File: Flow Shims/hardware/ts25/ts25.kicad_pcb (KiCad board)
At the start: 4 copper layers, 76.8 x 114 mm, 150 parts, among them J2 Nano-Fit, Q10 NVTFS5116PL, Q11 NVTFS5116PL, Q12 NVTFS5116PL, Q13 NVTFS5116PL, Q14 NVTFS5116PL, Q15 NVTFS5116PL, Q16 NVTFS5116PL, Q17 NVTFS5116PL, Q18 NVTFS5116PL, Q19 NVTFS5116PL, Q20 NVTFS5116PL, Q21 NVTFS5116PL, Q22 NVTFS5116PL, Q23 NVTFS5116PL, Q24 NVTFS5116PL, Q25 NVTFS5116PL, Q26 NVTFS5116PL, Q27 NVTFS5116PL, Q28 NVTFS5116PL, Q29 NVTFS5116PL, Q30 NVTFS5116PL, Q31 NVTFS5116PL, Q32 NVTFS5116PL, Q33 NVTFS5116PL, Q9 NVTFS5116PL, U1 ADG5206, U10 TMP1826NG, U11 TMP1826NG, U12 TMP1826NG, U13 TMP1826NG, U14 TMP1826NG, U15 TMP1826NG, U16 TMP1826NG, U17 TMP1826NG, U18 TMP1826NG, U19 TMP1826NG, U2 TMP1826NG, U20 TMP1826NG, U21 TMP1826NG, U22 TMP1826NG, U23 TMP1826NG, U24 TMP1826NG, U25 TMP1826NG, U26 TMP1826NG, U27 ADG5206, U3 TMP1826NG, U4 TMP1826NG, U5 TMP1826NG, U53 OPA196xDBV, U54 OPA196xDBV, U55 OPA196xDBV, U56 OPA196xDBV, U57 OPA196xDBV, U58 OPA196xDBV, U59 OPA196xDBV, U6 TMP1826NG, U60 OPA196xDBV, U61 OPA196xDBV, U62 OPA196xDBV, U63 OPA196xDBV, U64 OPA196xDBV, U65 OPA196xDBV, U66 OPA196xDBV, U67 OPA196xDBV, U68 OPA196xDBV, U69 OPA196xDBV, U7 TMP1826NG, U70 OPA196xDBV, U71 OPA196xDBV, U72 OPA196xDBV, U73 OPA196xDBV, U74 OPA196xDBV, U75 OPA196xDBV, U76 OPA196xDBV, U77 OPA196xDBV, U78 OPA196xDBV, U79 OPA196xDBV, U8 TMP1826NG, U9 TMP1826NG

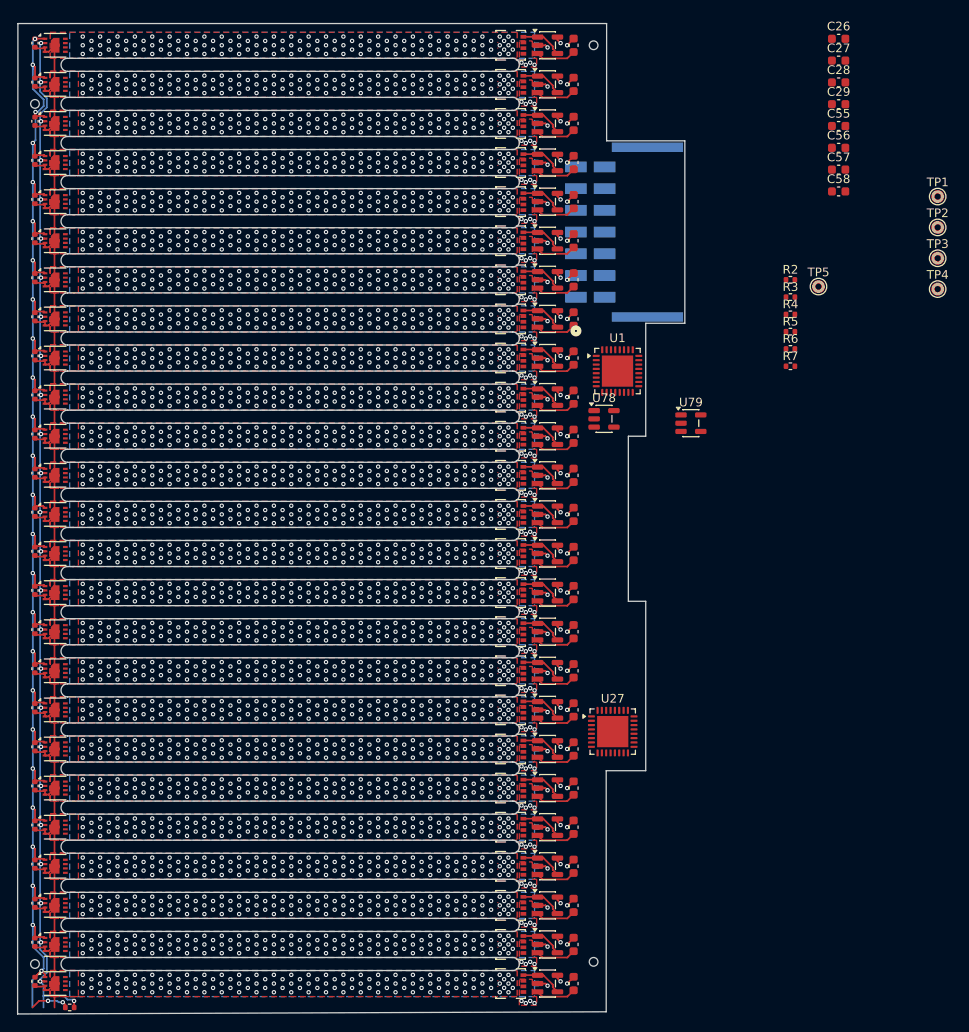
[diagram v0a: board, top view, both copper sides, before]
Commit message: DRC clean, single heater
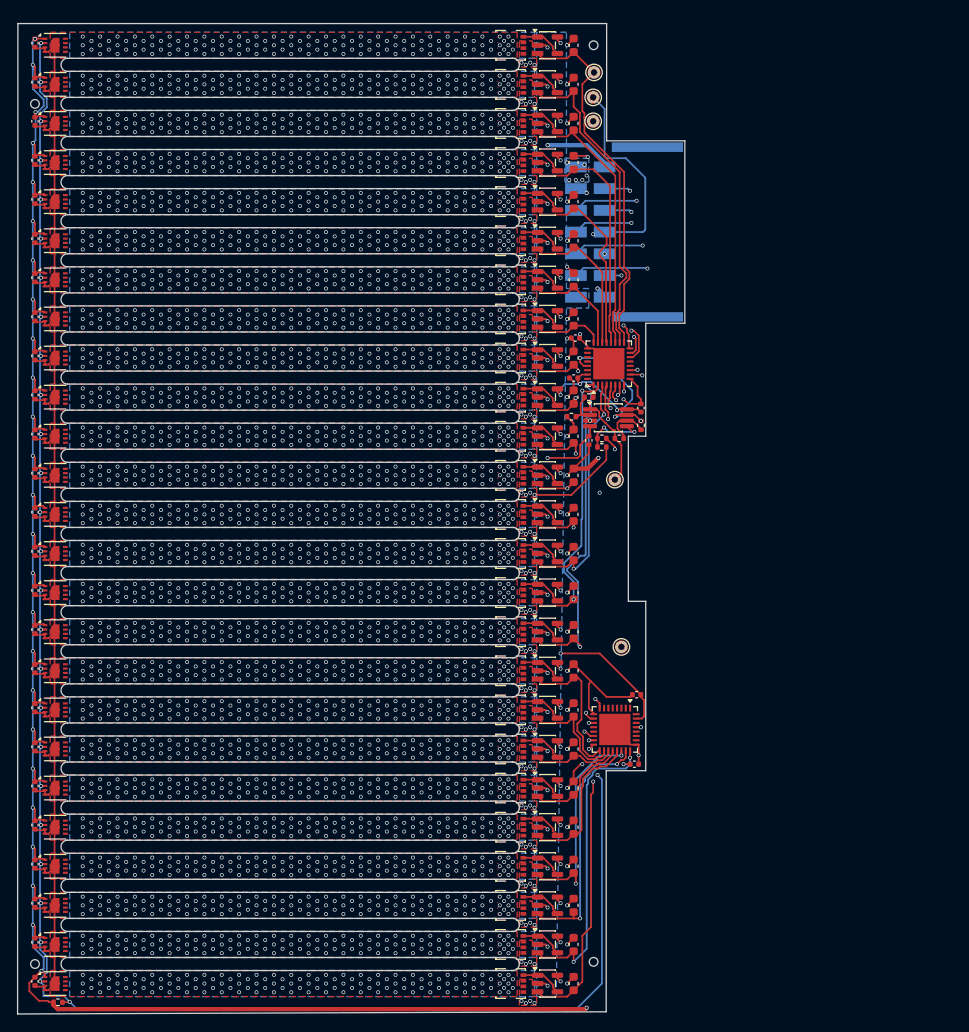
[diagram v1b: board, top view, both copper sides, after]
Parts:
- removed C55, C58: 100n, Capacitor_SMD:C_0603_1608Metric
- removed U78, U79: OPA196xDBV, Package_TO_SOT_SMD:SOT-23-5
- added U28: OPA2196xDGK, Package_SO:VSSOP-8_3x3mm_P0.65mm, F.Cu at (173.0, 86.4)
- C26, C27, C28, C29, C56, C57: footprint Capacitor_SMD:C_0603_1608Metric -> Capacitor_SMD:C_0402_1005Metric
- moved C26 86.7 mm to (176.0, 126.2)
- moved C28 74.2 mm to (176.2, 118.2)
- moved TP4 55.0 mm to (174.5, 112.8)
- moved TP3 45.1 mm to (173.8, 93.5)
- moved C27 44.0 mm to (169.2, 77.2)
- moved C29 43.9 mm to (169.0, 81.8)
- moved C57 42.4 mm to (170.8, 89.0), turned to -90 degrees
- moved TP2 42.4 mm to (171.2, 49.5)
- moved TP1 40.6 mm to (171.2, 52.2)
- moved C56 37.6 mm to (176.8, 85.2), turned to 90 degrees
- moved TP5 35.7 mm to (171.3, 46.6)
- moved R3 28.7 mm to (168.8, 86.2)
- moved R2 26.8 mm to (170.8, 84.0)
- moved R4 26.0 mm to (172.2, 88.8), turned to 180 degrees
- moved R5 25.4 mm to (172.2, 89.8)
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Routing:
- net GND: track 217.1 -> 375.3 mm, vias 3275 -> 3281
- net +3.3V: track 187.4 -> 342.4 mm
- net -15V: track 31.0 -> 182.9 mm, vias 25 -> 29
- net /VTEMP: track 131.7 -> 278.2 mm, vias 26 -> 29
- net +15V: track 21.3 -> 164.7 mm, vias 25 -> 29
- net /A0: track 0.00 -> 76.0 mm, vias 0 -> 3
- net /A1: track 0.00 -> 74.3 mm, vias 0 -> 3
- net /EN1: track 0.00 -> 73.8 mm, vias 0 -> 2
- net /A2: track 0.00 -> 67.8 mm, vias 0 -> 3
- net /A3: track 0.00 -> 65.4 mm, vias 0 -> 3
- net /VG: track 0.00 -> 54.3 mm, vias 0 -> 4
- net /VGIN: track 0.00 -> 47.2 mm, vias 0 -> 2
- net /VG1: track 4.67 -> 42.6 mm
- net /VG25: track 4.67 -> 40.6 mm, vias 0 -> 2
- net /VG16: track 4.67 -> 39.2 mm, vias 0 -> 2
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- added copper zone on B.Cu, net VD
- added copper zone on In1.Cu, net VD

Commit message: Building code for heater control PID loops
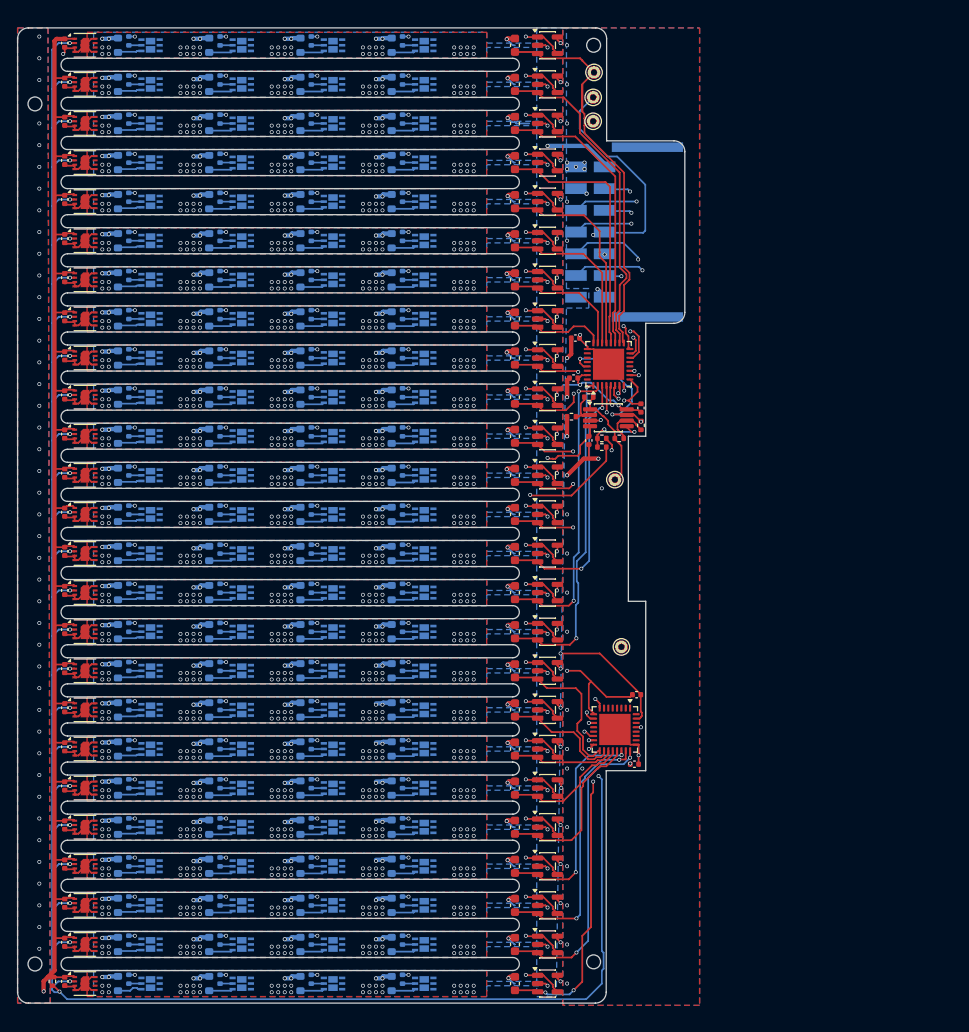
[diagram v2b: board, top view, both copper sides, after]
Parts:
- removed Q10, Q11, Q12, Q13, Q14, Q15, Q16, Q17, Q18, Q19, Q20, Q21, Q22, Q23, Q24, Q25, Q26, Q27, Q28, Q29, Q30, Q31, Q32, Q33, Q9: NVTFS5116PL, thermalshims:WDFN8_511AB_ONS_OSI
- added R10: 5, Resistor_SMD:R_0603_1608Metric, B.Cu at (116.6, 52.5)
- added R100: 10, Resistor_SMD:R_0402_1005Metric, B.Cu at (128.3, 137.5)
- added R101: 5, Resistor_SMD:R_0603_1608Metric, B.Cu at (127.1, 138.0)
- added R102: 10, Resistor_SMD:R_0402_1005Metric, B.Cu at (128.3, 142.0)
- added R103: 5, Resistor_SMD:R_0603_1608Metric, B.Cu at (127.1, 142.5)
- added R104: 10, Resistor_SMD:R_0402_1005Metric, B.Cu at (128.3, 146.5)
- added R105: 5, Resistor_SMD:R_0603_1608Metric, B.Cu at (127.1, 147.0)
- added R106: 10, Resistor_SMD:R_0402_1005Metric, B.Cu at (128.3, 151.0)
- added R107: 5, Resistor_SMD:R_0603_1608Metric, B.Cu at (127.1, 151.5)
- added R108: 10, Resistor_SMD:R_0402_1005Metric, B.Cu at (138.8, 43.0)
- added R109: 5, Resistor_SMD:R_0603_1608Metric, B.Cu at (137.6, 43.5)
- added R11: 5, Resistor_SMD:R_0603_1608Metric, B.Cu at (116.6, 57.0)
- added R110: 10, Resistor_SMD:R_0402_1005Metric, B.Cu at (138.8, 47.5)
- added R111: 5, Resistor_SMD:R_0603_1608Metric, B.Cu at (137.6, 48.0)
- added R112: 10, Resistor_SMD:R_0402_1005Metric, B.Cu at (138.8, 52.0)
- added R113: 5, Resistor_SMD:R_0603_1608Metric, B.Cu at (137.6, 52.5)
- added R114: 10, Resistor_SMD:R_0402_1005Metric, B.Cu at (138.8, 56.5)
- added R115: 5, Resistor_SMD:R_0603_1608Metric, B.Cu at (137.6, 57.0)
- added R116: 10, Resistor_SMD:R_0402_1005Metric, B.Cu at (138.8, 61.0)
- added R117: 5, Resistor_SMD:R_0603_1608Metric, B.Cu at (137.6, 61.5)
- added R118: 10, Resistor_SMD:R_0402_1005Metric, B.Cu at (138.8, 65.5)
- added R119: 5, Resistor_SMD:R_0603_1608Metric, B.Cu at (137.6, 66.0)
- added R12: 5, Resistor_SMD:R_0603_1608Metric, B.Cu at (116.6, 61.5)
- added R120: 10, Resistor_SMD:R_0402_1005Metric, B.Cu at (138.8, 70.0)
- added R121: 5, Resistor_SMD:R_0603_1608Metric, B.Cu at (137.6, 70.5)
- added R122: 10, Resistor_SMD:R_0402_1005Metric, B.Cu at (138.8, 74.5)
- added R123: 5, Resistor_SMD:R_0603_1608Metric, B.Cu at (137.6, 75.0)
- added R124: 10, Resistor_SMD:R_0402_1005Metric, B.Cu at (138.8, 79.0)
- added R125: 5, Resistor_SMD:R_0603_1608Metric, B.Cu at (137.6, 79.5)
- added R126: 10, Resistor_SMD:R_0402_1005Metric, B.Cu at (138.8, 83.5)
- added R127: 5, Resistor_SMD:R_0603_1608Metric, B.Cu at (137.6, 84.0)
- added R128: 10, Resistor_SMD:R_0402_1005Metric, B.Cu at (138.8, 88.0)
- added R129: 5, Resistor_SMD:R_0603_1608Metric, B.Cu at (137.6, 88.5)
- added R13: 5, Resistor_SMD:R_0603_1608Metric, B.Cu at (116.6, 66.0)
- added R130: 10, Resistor_SMD:R_0402_1005Metric, B.Cu at (138.8, 92.5)
- added R131: 5, Resistor_SMD:R_0603_1608Metric, B.Cu at (137.6, 93.0)
- added R132: 10, Resistor_SMD:R_0402_1005Metric, B.Cu at (138.8, 97.0)
- added R133: 5, Resistor_SMD:R_0603_1608Metric, B.Cu at (137.6, 97.5)
- added R134: 10, Resistor_SMD:R_0402_1005Metric, B.Cu at (138.8, 101.5)
- added R135: 5, Resistor_SMD:R_0603_1608Metric, B.Cu at (137.6, 102.0)
- added R136: 10, Resistor_SMD:R_0402_1005Metric, B.Cu at (138.8, 106.0)
- added R137: 5, Resistor_SMD:R_0603_1608Metric, B.Cu at (137.6, 106.5)
- added R138: 10, Resistor_SMD:R_0402_1005Metric, B.Cu at (138.8, 110.5)
- added R139: 5, Resistor_SMD:R_0603_1608Metric, B.Cu at (137.6, 111.0)
- added R14: 5, Resistor_SMD:R_0603_1608Metric, B.Cu at (116.6, 70.5)
- added R140: 10, Resistor_SMD:R_0402_1005Metric, B.Cu at (138.8, 115.0)
- added R141: 5, Resistor_SMD:R_0603_1608Metric, B.Cu at (137.6, 115.5)
- added R142: 10, Resistor_SMD:R_0402_1005Metric, B.Cu at (138.8, 119.5)
- added R143: 5, Resistor_SMD:R_0603_1608Metric, B.Cu at (137.6, 120.0)
- added R144: 10, Resistor_SMD:R_0402_1005Metric, B.Cu at (138.8, 124.0)
- added R145: 5, Resistor_SMD:R_0603_1608Metric, B.Cu at (137.6, 124.5)
- added R146: 10, Resistor_SMD:R_0402_1005Metric, B.Cu at (138.8, 128.5)
- added R147: 5, Resistor_SMD:R_0603_1608Metric, B.Cu at (137.6, 129.0)
- added R148: 10, Resistor_SMD:R_0402_1005Metric, B.Cu at (138.8, 133.0)
- added R149: 5, Resistor_SMD:R_0603_1608Metric, B.Cu at (137.6, 133.5)
- added R15: 5, Resistor_SMD:R_0603_1608Metric, B.Cu at (116.6, 75.0)
- added R150: 10, Resistor_SMD:R_0402_1005Metric, B.Cu at (138.8, 137.5)
- added R151: 5, Resistor_SMD:R_0603_1608Metric, B.Cu at (137.6, 138.0)
- added R152: 10, Resistor_SMD:R_0402_1005Metric, B.Cu at (138.8, 142.0)
- added R153: 5, Resistor_SMD:R_0603_1608Metric, B.Cu at (137.6, 142.5)
- added R154: 10, Resistor_SMD:R_0402_1005Metric, B.Cu at (138.8, 146.5)
- added R155: 5, Resistor_SMD:R_0603_1608Metric, B.Cu at (137.6, 147.0)
- added R156: 10, Resistor_SMD:R_0402_1005Metric, B.Cu at (138.8, 151.0)
- added R157: 5, Resistor_SMD:R_0603_1608Metric, B.Cu at (137.6, 151.5)
- added R158: 10, Resistor_SMD:R_0402_1005Metric, B.Cu at (149.3, 43.0)
- added R159: 5, Resistor_SMD:R_0603_1608Metric, B.Cu at (148.1, 43.5)
- added R16: 5, Resistor_SMD:R_0603_1608Metric, B.Cu at (116.6, 79.5)
- added R160: 10, Resistor_SMD:R_0402_1005Metric, B.Cu at (149.3, 47.5)
- added R161: 5, Resistor_SMD:R_0603_1608Metric, B.Cu at (148.1, 48.0)
- added R162: 10, Resistor_SMD:R_0402_1005Metric, B.Cu at (149.3, 52.0)
- added R163: 5, Resistor_SMD:R_0603_1608Metric, B.Cu at (148.1, 52.5)
- added R164: 10, Resistor_SMD:R_0402_1005Metric, B.Cu at (149.3, 56.5)
- added R165: 5, Resistor_SMD:R_0603_1608Metric, B.Cu at (148.1, 57.0)
- added R166: 10, Resistor_SMD:R_0402_1005Metric, B.Cu at (149.3, 61.0)
- added R167: 5, Resistor_SMD:R_0603_1608Metric, B.Cu at (148.1, 61.5)
- added R168: 10, Resistor_SMD:R_0402_1005Metric, B.Cu at (149.3, 65.5)
- added R169: 5, Resistor_SMD:R_0603_1608Metric, B.Cu at (148.1, 66.0)
- added R17: 5, Resistor_SMD:R_0603_1608Metric, B.Cu at (116.6, 84.0)
- added R170: 10, Resistor_SMD:R_0402_1005Metric, B.Cu at (149.3, 70.0)
- added R171: 5, Resistor_SMD:R_0603_1608Metric, B.Cu at (148.1, 70.5)
- added R172: 10, Resistor_SMD:R_0402_1005Metric, B.Cu at (149.3, 74.5)
- added R173: 5, Resistor_SMD:R_0603_1608Metric, B.Cu at (148.1, 75.0)
- added R174: 10, Resistor_SMD:R_0402_1005Metric, B.Cu at (149.3, 79.0)
- added R175: 5, Resistor_SMD:R_0603_1608Metric, B.Cu at (148.1, 79.5)
- added R176: 10, Resistor_SMD:R_0402_1005Metric, B.Cu at (149.3, 83.5)
- added R177: 5, Resistor_SMD:R_0603_1608Metric, B.Cu at (148.1, 84.0)
- added R178: 10, Resistor_SMD:R_0402_1005Metric, B.Cu at (149.3, 88.0)
- added R179: 5, Resistor_SMD:R_0603_1608Metric, B.Cu at (148.1, 88.5)
- added R18: 5, Resistor_SMD:R_0603_1608Metric, B.Cu at (116.6, 88.5)
- added R180: 10, Resistor_SMD:R_0402_1005Metric, B.Cu at (149.3, 92.5)
- added R181: 5, Resistor_SMD:R_0603_1608Metric, B.Cu at (148.1, 93.0)
- added R182: 10, Resistor_SMD:R_0402_1005Metric, B.Cu at (149.3, 97.0)
- added R183: 5, Resistor_SMD:R_0603_1608Metric, B.Cu at (148.1, 97.5)
- added R184: 10, Resistor_SMD:R_0402_1005Metric, B.Cu at (149.3, 101.5)
- added R185: 5, Resistor_SMD:R_0603_1608Metric, B.Cu at (148.1, 102.0)
- added R186: 10, Resistor_SMD:R_0402_1005Metric, B.Cu at (149.3, 106.0)
- added R187: 5, Resistor_SMD:R_0603_1608Metric, B.Cu at (148.1, 106.5)
- added R188: 10, Resistor_SMD:R_0402_1005Metric, B.Cu at (149.3, 110.5)
- added R189: 5, Resistor_SMD:R_0603_1608Metric, B.Cu at (148.1, 111.0)
- added R19: 5, Resistor_SMD:R_0603_1608Metric, B.Cu at (116.6, 93.0)
- added R190: 10, Resistor_SMD:R_0402_1005Metric, B.Cu at (149.3, 115.0)
- added R191: 5, Resistor_SMD:R_0603_1608Metric, B.Cu at (148.1, 115.5)
- added R192: 10, Resistor_SMD:R_0402_1005Metric, B.Cu at (149.3, 119.5)
- added R193: 5, Resistor_SMD:R_0603_1608Metric, B.Cu at (148.1, 120.0)
- added R194: 10, Resistor_SMD:R_0402_1005Metric, B.Cu at (149.3, 124.0)
- added R195: 5, Resistor_SMD:R_0603_1608Metric, B.Cu at (148.1, 124.5)
- added R196: 10, Resistor_SMD:R_0402_1005Metric, B.Cu at (149.3, 128.5)
- added R197: 5, Resistor_SMD:R_0603_1608Metric, B.Cu at (148.1, 129.0)
- added R198: 10, Resistor_SMD:R_0402_1005Metric, B.Cu at (149.3, 133.0)
- added R199: 5, Resistor_SMD:R_0603_1608Metric, B.Cu at (148.1, 133.5)
- added R20: 5, Resistor_SMD:R_0603_1608Metric, B.Cu at (116.6, 97.5)
- added R200: 10, Resistor_SMD:R_0402_1005Metric, B.Cu at (149.3, 137.5)
- added R201: 5, Resistor_SMD:R_0603_1608Metric, B.Cu at (148.1, 138.0)
- added R202: 10, Resistor_SMD:R_0402_1005Metric, B.Cu at (149.3, 142.0)
- added R203: 5, Resistor_SMD:R_0603_1608Metric, B.Cu at (148.1, 142.5)
- added R204: 10, Resistor_SMD:R_0402_1005Metric, B.Cu at (149.3, 146.5)
- added R205: 5, Resistor_SMD:R_0603_1608Metric, B.Cu at (148.1, 147.0)
- added R206: 10, Resistor_SMD:R_0402_1005Metric, B.Cu at (149.3, 151.0)
- added R207: 5, Resistor_SMD:R_0603_1608Metric, B.Cu at (148.1, 151.5)
- added R21: 5, Resistor_SMD:R_0603_1608Metric, B.Cu at (116.6, 102.0)
- added R22: 5, Resistor_SMD:R_0603_1608Metric, B.Cu at (116.6, 106.5)
- added R23: 5, Resistor_SMD:R_0603_1608Metric, B.Cu at (116.6, 111.0)
- added R24: 5, Resistor_SMD:R_0603_1608Metric, B.Cu at (116.6, 115.5)
- added R25: 5, Resistor_SMD:R_0603_1608Metric, B.Cu at (116.6, 120.0)
- added R26: 5, Resistor_SMD:R_0603_1608Metric, B.Cu at (116.6, 124.5)
- added R27: 5, Resistor_SMD:R_0603_1608Metric, B.Cu at (116.6, 129.0)
- added R28: 5, Resistor_SMD:R_0603_1608Metric, B.Cu at (116.6, 133.5)
- added R29: 5, Resistor_SMD:R_0603_1608Metric, B.Cu at (116.6, 138.0)
- added R30: 5, Resistor_SMD:R_0603_1608Metric, B.Cu at (116.6, 142.5)
- added R31: 5, Resistor_SMD:R_0603_1608Metric, B.Cu at (116.6, 147.0)
- added R32: 5, Resistor_SMD:R_0603_1608Metric, B.Cu at (116.6, 151.5)
- added R33: 10, Resistor_SMD:R_0402_1005Metric, B.Cu at (117.8, 43.0)
- added R34: 10, Resistor_SMD:R_0402_1005Metric, B.Cu at (117.8, 47.5)
- added R35: 10, Resistor_SMD:R_0402_1005Metric, B.Cu at (117.8, 52.0)
- added R36: 10, Resistor_SMD:R_0402_1005Metric, B.Cu at (117.8, 56.5)
- added R37: 10, Resistor_SMD:R_0402_1005Metric, B.Cu at (117.8, 61.0)
- added R38: 10, Resistor_SMD:R_0402_1005Metric, B.Cu at (117.8, 65.5)
- added R39: 10, Resistor_SMD:R_0402_1005Metric, B.Cu at (117.8, 70.0)
- added R40: 10, Resistor_SMD:R_0402_1005Metric, B.Cu at (117.8, 74.5)
- added R41: 10, Resistor_SMD:R_0402_1005Metric, B.Cu at (117.8, 79.0)
- added R42: 10, Resistor_SMD:R_0402_1005Metric, B.Cu at (117.8, 83.5)
- added R43: 10, Resistor_SMD:R_0402_1005Metric, B.Cu at (117.8, 88.0)
- added R44: 10, Resistor_SMD:R_0402_1005Metric, B.Cu at (117.8, 92.5)
- added R45: 10, Resistor_SMD:R_0402_1005Metric, B.Cu at (117.8, 97.0)
- added R46: 10, Resistor_SMD:R_0402_1005Metric, B.Cu at (117.8, 101.5)
- added R47: 10, Resistor_SMD:R_0402_1005Metric, B.Cu at (117.8, 106.0)
- added R48: 10, Resistor_SMD:R_0402_1005Metric, B.Cu at (117.8, 110.5)
- added R49: 10, Resistor_SMD:R_0402_1005Metric, B.Cu at (117.8, 115.0)
- added R50: 10, Resistor_SMD:R_0402_1005Metric, B.Cu at (117.8, 119.5)
- added R51: 10, Resistor_SMD:R_0402_1005Metric, B.Cu at (117.8, 124.0)
- added R52: 10, Resistor_SMD:R_0402_1005Metric, B.Cu at (117.8, 128.5)
- added R53: 10, Resistor_SMD:R_0402_1005Metric, B.Cu at (117.8, 133.0)
- added R54: 10, Resistor_SMD:R_0402_1005Metric, B.Cu at (117.8, 137.5)
- added R55: 10, Resistor_SMD:R_0402_1005Metric, B.Cu at (117.8, 142.0)
- added R56: 10, Resistor_SMD:R_0402_1005Metric, B.Cu at (117.8, 146.5)
- added R57: 10, Resistor_SMD:R_0402_1005Metric, B.Cu at (117.8, 151.0)
- added R58: 10, Resistor_SMD:R_0402_1005Metric, B.Cu at (128.3, 43.0)
- added R59: 5, Resistor_SMD:R_0603_1608Metric, B.Cu at (127.1, 43.5)
- added R60: 10, Resistor_SMD:R_0402_1005Metric, B.Cu at (128.3, 47.5)
- added R61: 5, Resistor_SMD:R_0603_1608Metric, B.Cu at (127.1, 48.0)
- added R62: 10, Resistor_SMD:R_0402_1005Metric, B.Cu at (128.3, 52.0)
- added R63: 5, Resistor_SMD:R_0603_1608Metric, B.Cu at (127.1, 52.5)
- added R64: 10, Resistor_SMD:R_0402_1005Metric, B.Cu at (128.3, 56.5)
- added R65: 5, Resistor_SMD:R_0603_1608Metric, B.Cu at (127.1, 57.0)
- added R66: 10, Resistor_SMD:R_0402_1005Metric, B.Cu at (128.3, 61.0)
- added R67: 5, Resistor_SMD:R_0603_1608Metric, B.Cu at (127.1, 61.5)
- added R68: 10, Resistor_SMD:R_0402_1005Metric, B.Cu at (128.3, 65.5)
- added R69: 5, Resistor_SMD:R_0603_1608Metric, B.Cu at (127.1, 66.0)
- added R70: 10, Resistor_SMD:R_0402_1005Metric, B.Cu at (128.3, 70.0)
- added R71: 5, Resistor_SMD:R_0603_1608Metric, B.Cu at (127.1, 70.5)
- added R72: 10, Resistor_SMD:R_0402_1005Metric, B.Cu at (128.3, 74.5)
- added R73: 5, Resistor_SMD:R_0603_1608Metric, B.Cu at (127.1, 75.0)
- added R74: 10, Resistor_SMD:R_0402_1005Metric, B.Cu at (128.3, 79.0)
- added R75: 5, Resistor_SMD:R_0603_1608Metric, B.Cu at (127.1, 79.5)
- added R76: 10, Resistor_SMD:R_0402_1005Metric, B.Cu at (128.3, 83.5)
- added R77: 5, Resistor_SMD:R_0603_1608Metric, B.Cu at (127.1, 84.0)
- added R78: 10, Resistor_SMD:R_0402_1005Metric, B.Cu at (128.3, 88.0)
- added R79: 5, Resistor_SMD:R_0603_1608Metric, B.Cu at (127.1, 88.5)
- added R8: 5, Resistor_SMD:R_0603_1608Metric, B.Cu at (116.6, 43.5)
- added R80: 10, Resistor_SMD:R_0402_1005Metric, B.Cu at (128.3, 92.5)
- added R81: 5, Resistor_SMD:R_0603_1608Metric, B.Cu at (127.1, 93.0)
- added R82: 10, Resistor_SMD:R_0402_1005Metric, B.Cu at (128.3, 97.0)
- added R83: 5, Resistor_SMD:R_0603_1608Metric, B.Cu at (127.1, 97.5)
- added R84: 10, Resistor_SMD:R_0402_1005Metric, B.Cu at (128.3, 101.5)
- added R85: 5, Resistor_SMD:R_0603_1608Metric, B.Cu at (127.1, 102.0)
- added R86: 10, Resistor_SMD:R_0402_1005Metric, B.Cu at (128.3, 106.0)
- added R87: 5, Resistor_SMD:R_0603_1608Metric, B.Cu at (127.1, 106.5)
- added R88: 10, Resistor_SMD:R_0402_1005Metric, B.Cu at (128.3, 110.5)
- added R89: 5, Resistor_SMD:R_0603_1608Metric, B.Cu at (127.1, 111.0)
- added R9: 5, Resistor_SMD:R_0603_1608Metric, B.Cu at (116.6, 48.0)
- added R90: 10, Resistor_SMD:R_0402_1005Metric, B.Cu at (128.3, 115.0)
- added R91: 5, Resistor_SMD:R_0603_1608Metric, B.Cu at (127.1, 115.5)
- added R92: 10, Resistor_SMD:R_0402_1005Metric, B.Cu at (128.3, 119.5)
- added R93: 5, Resistor_SMD:R_0603_1608Metric, B.Cu at (127.1, 120.0)
- added R94: 10, Resistor_SMD:R_0402_1005Metric, B.Cu at (128.3, 124.0)
- added R95: 5, Resistor_SMD:R_0603_1608Metric, B.Cu at (127.1, 124.5)
- added R96: 10, Resistor_SMD:R_0402_1005Metric, B.Cu at (128.3, 128.5)
- added R97: 5, Resistor_SMD:R_0603_1608Metric, B.Cu at (127.1, 129.0)
- added R98: 10, Resistor_SMD:R_0402_1005Metric, B.Cu at (128.3, 133.0)
- added R99: 5, Resistor_SMD:R_0603_1608Metric, B.Cu at (127.1, 133.5)
- added U100: ~, thermalshims:WDFN6_2x2_ONS-M, B.Cu at (130.8, 138.0)
- added U101: ~, thermalshims:WDFN6_2x2_ONS-M, B.Cu at (130.8, 142.5)
- added U102: ~, thermalshims:WDFN6_2x2_ONS-M, B.Cu at (130.8, 147.0)
- added U103: ~, thermalshims:WDFN6_2x2_ONS-M, B.Cu at (130.8, 151.5)
- added U104: ~, thermalshims:WDFN6_2x2_ONS-M, B.Cu at (141.3, 43.5)
- added U105: ~, thermalshims:WDFN6_2x2_ONS-M, B.Cu at (141.3, 48.0)
- added U106: ~, thermalshims:WDFN6_2x2_ONS-M, B.Cu at (141.3, 52.5)
- added U107: ~, thermalshims:WDFN6_2x2_ONS-M, B.Cu at (141.3, 57.0)
- added U108: ~, thermalshims:WDFN6_2x2_ONS-M, B.Cu at (141.3, 61.5)
- added U109: ~, thermalshims:WDFN6_2x2_ONS-M, B.Cu at (141.3, 66.0)
- added U110: ~, thermalshims:WDFN6_2x2_ONS-M, B.Cu at (141.3, 70.5)
- added U111: ~, thermalshims:WDFN6_2x2_ONS-M, B.Cu at (141.3, 75.0)
- added U112: ~, thermalshims:WDFN6_2x2_ONS-M, B.Cu at (141.3, 79.5)
- added U113: ~, thermalshims:WDFN6_2x2_ONS-M, B.Cu at (141.3, 84.0)
- added U114: ~, thermalshims:WDFN6_2x2_ONS-M, B.Cu at (141.3, 88.5)
- added U115: ~, thermalshims:WDFN6_2x2_ONS-M, B.Cu at (141.3, 93.0)
- added U116: ~, thermalshims:WDFN6_2x2_ONS-M, B.Cu at (141.3, 97.5)
- added U117: ~, thermalshims:WDFN6_2x2_ONS-M, B.Cu at (141.3, 102.0)
- added U118: ~, thermalshims:WDFN6_2x2_ONS-M, B.Cu at (141.3, 106.5)
- added U119: ~, thermalshims:WDFN6_2x2_ONS-M, B.Cu at (141.3, 111.0)
- added U120: ~, thermalshims:WDFN6_2x2_ONS-M, B.Cu at (141.3, 115.5)
- added U121: ~, thermalshims:WDFN6_2x2_ONS-M, B.Cu at (141.3, 120.0)
- added U122: ~, thermalshims:WDFN6_2x2_ONS-M, B.Cu at (141.3, 124.5)
- added U123: ~, thermalshims:WDFN6_2x2_ONS-M, B.Cu at (141.3, 129.0)
- added U124: ~, thermalshims:WDFN6_2x2_ONS-M, B.Cu at (141.3, 133.5)
- added U125: ~, thermalshims:WDFN6_2x2_ONS-M, B.Cu at (141.3, 138.0)
- added U126: ~, thermalshims:WDFN6_2x2_ONS-M, B.Cu at (141.3, 142.5)
- added U127: ~, thermalshims:WDFN6_2x2_ONS-M, B.Cu at (141.3, 147.0)
- added U128: ~, thermalshims:WDFN6_2x2_ONS-M, B.Cu at (141.3, 151.5)
- added U129: ~, thermalshims:WDFN6_2x2_ONS-M, B.Cu at (151.8, 43.5)
- added U130: ~, thermalshims:WDFN6_2x2_ONS-M, B.Cu at (151.8, 48.0)
- added U131: ~, thermalshims:WDFN6_2x2_ONS-M, B.Cu at (151.8, 52.5)
- added U132: ~, thermalshims:WDFN6_2x2_ONS-M, B.Cu at (151.8, 57.0)
- added U133: ~, thermalshims:WDFN6_2x2_ONS-M, B.Cu at (151.8, 61.5)
- added U134: ~, thermalshims:WDFN6_2x2_ONS-M, B.Cu at (151.8, 66.0)
- added U135: ~, thermalshims:WDFN6_2x2_ONS-M, B.Cu at (151.8, 70.5)
- added U136: ~, thermalshims:WDFN6_2x2_ONS-M, B.Cu at (151.8, 75.0)
- added U137: ~, thermalshims:WDFN6_2x2_ONS-M, B.Cu at (151.8, 79.5)
- added U138: ~, thermalshims:WDFN6_2x2_ONS-M, B.Cu at (151.8, 84.0)
- added U139: ~, thermalshims:WDFN6_2x2_ONS-M, B.Cu at (151.8, 88.5)
- added U140: ~, thermalshims:WDFN6_2x2_ONS-M, B.Cu at (151.8, 93.0)
- added U141: ~, thermalshims:WDFN6_2x2_ONS-M, B.Cu at (151.8, 97.5)
- added U142: ~, thermalshims:WDFN6_2x2_ONS-M, B.Cu at (151.8, 102.0)
- added U143: ~, thermalshims:WDFN6_2x2_ONS-M, B.Cu at (151.8, 106.5)
- added U144: ~, thermalshims:WDFN6_2x2_ONS-M, B.Cu at (151.8, 111.0)
- added U145: ~, thermalshims:WDFN6_2x2_ONS-M, B.Cu at (151.8, 115.5)
- added U146: ~, thermalshims:WDFN6_2x2_ONS-M, B.Cu at (151.8, 120.0)
- added U147: ~, thermalshims:WDFN6_2x2_ONS-M, B.Cu at (151.8, 124.5)
- added U148: ~, thermalshims:WDFN6_2x2_ONS-M, B.Cu at (151.8, 129.0)
- added U149: ~, thermalshims:WDFN6_2x2_ONS-M, B.Cu at (151.8, 133.5)
- added U150: ~, thermalshims:WDFN6_2x2_ONS-M, B.Cu at (151.8, 138.0)
- added U151: ~, thermalshims:WDFN6_2x2_ONS-M, B.Cu at (151.8, 142.5)
- added U152: ~, thermalshims:WDFN6_2x2_ONS-M, B.Cu at (151.8, 147.0)
- added U153: ~, thermalshims:WDFN6_2x2_ONS-M, B.Cu at (151.8, 151.5)
- added U29: ~, thermalshims:WDFN6_2x2_ONS-M, B.Cu at (120.3, 43.5)
- added U30: ~, thermalshims:WDFN6_2x2_ONS-M, B.Cu at (120.3, 48.0)
- added U31: ~, thermalshims:WDFN6_2x2_ONS-M, B.Cu at (120.3, 52.5)
- added U32: ~, thermalshims:WDFN6_2x2_ONS-M, B.Cu at (120.3, 57.0)
- added U33: ~, thermalshims:WDFN6_2x2_ONS-M, B.Cu at (120.3, 61.5)
- added U34: ~, thermalshims:WDFN6_2x2_ONS-M, B.Cu at (120.3, 66.0)
- added U35: ~, thermalshims:WDFN6_2x2_ONS-M, B.Cu at (120.3, 70.5)
- added U36: ~, thermalshims:WDFN6_2x2_ONS-M, B.Cu at (120.3, 75.0)
- added U37: ~, thermalshims:WDFN6_2x2_ONS-M, B.Cu at (120.3, 79.5)
- added U38: ~, thermalshims:WDFN6_2x2_ONS-M, B.Cu at (120.3, 84.0)
- added U39: ~, thermalshims:WDFN6_2x2_ONS-M, B.Cu at (120.3, 88.5)
- added U40: ~, thermalshims:WDFN6_2x2_ONS-M, B.Cu at (120.3, 93.0)
- added U41: ~, thermalshims:WDFN6_2x2_ONS-M, B.Cu at (120.3, 97.5)
- added U42: ~, thermalshims:WDFN6_2x2_ONS-M, B.Cu at (120.3, 102.0)
- added U43: ~, thermalshims:WDFN6_2x2_ONS-M, B.Cu at (120.3, 106.5)
- added U44: ~, thermalshims:WDFN6_2x2_ONS-M, B.Cu at (120.3, 111.0)
- added U45: ~, thermalshims:WDFN6_2x2_ONS-M, B.Cu at (120.3, 115.5)
- added U46: ~, thermalshims:WDFN6_2x2_ONS-M, B.Cu at (120.3, 120.0)
- added U47: ~, thermalshims:WDFN6_2x2_ONS-M, B.Cu at (120.3, 124.5)
- added U48: ~, thermalshims:WDFN6_2x2_ONS-M, B.Cu at (120.3, 129.0)
- added U49: ~, thermalshims:WDFN6_2x2_ONS-M, B.Cu at (120.3, 133.5)
- added U50: ~, thermalshims:WDFN6_2x2_ONS-M, B.Cu at (120.3, 138.0)
- added U51: ~, thermalshims:WDFN6_2x2_ONS-M, B.Cu at (120.3, 142.5)
- added U52: ~, thermalshims:WDFN6_2x2_ONS-M, B.Cu at (120.3, 147.0)
- added U78: ~, thermalshims:WDFN6_2x2_ONS-M, B.Cu at (120.3, 151.5)
- added U79: ~, thermalshims:WDFN6_2x2_ONS-M, B.Cu at (130.8, 43.5)
- added U80: ~, thermalshims:WDFN6_2x2_ONS-M, B.Cu at (130.8, 48.0)
- added U81: ~, thermalshims:WDFN6_2x2_ONS-M, B.Cu at (130.8, 52.5)
- added U82: ~, thermalshims:WDFN6_2x2_ONS-M, B.Cu at (130.8, 57.0)
- added U83: ~, thermalshims:WDFN6_2x2_ONS-M, B.Cu at (130.8, 61.5)
- added U84: ~, thermalshims:WDFN6_2x2_ONS-M, B.Cu at (130.8, 66.0)
- added U85: ~, thermalshims:WDFN6_2x2_ONS-M, B.Cu at (130.8, 70.5)
- added U86: ~, thermalshims:WDFN6_2x2_ONS-M, B.Cu at (130.8, 75.0)
- added U87: ~, thermalshims:WDFN6_2x2_ONS-M, B.Cu at (130.8, 79.5)
- added U88: ~, thermalshims:WDFN6_2x2_ONS-M, B.Cu at (130.8, 84.0)
- added U89: ~, thermalshims:WDFN6_2x2_ONS-M, B.Cu at (130.8, 88.5)
- added U90: ~, thermalshims:WDFN6_2x2_ONS-M, B.Cu at (130.8, 93.0)
- added U91: ~, thermalshims:WDFN6_2x2_ONS-M, B.Cu at (130.8, 97.5)
- added U92: ~, thermalshims:WDFN6_2x2_ONS-M, B.Cu at (130.8, 102.0)
- added U93: ~, thermalshims:WDFN6_2x2_ONS-M, B.Cu at (130.8, 106.5)
- added U94: ~, thermalshims:WDFN6_2x2_ONS-M, B.Cu at (130.8, 111.0)
- added U95: ~, thermalshims:WDFN6_2x2_ONS-M, B.Cu at (130.8, 115.5)
- added U96: ~, thermalshims:WDFN6_2x2_ONS-M, B.Cu at (130.8, 120.0)
- added U97: ~, thermalshims:WDFN6_2x2_ONS-M, B.Cu at (130.8, 124.5)
- added U98: ~, thermalshims:WDFN6_2x2_ONS-M, B.Cu at (130.8, 129.0)
- added U99: ~, thermalshims:WDFN6_2x2_ONS-M, B.Cu at (130.8, 133.5)
- moved C30 6.75 mm to (162.2, 43.5)
- moved C31 6.75 mm to (162.2, 48.0)
- moved C32 6.75 mm to (162.2, 52.5)
- moved C33 6.75 mm to (162.2, 57.0)
- moved C34 6.75 mm to (162.2, 61.5)
- moved C35 6.75 mm to (162.2, 66.0)
- moved C36 6.75 mm to (162.2, 70.5)
- moved C37 6.75 mm to (162.2, 75.0)
- moved C38 6.75 mm to (162.2, 79.5)
- moved C39 6.75 mm to (162.2, 84.0)
- moved C40 6.75 mm to (162.2, 88.5)
- moved C41 6.75 mm to (162.2, 93.0)
- moved C42 6.75 mm to (162.2, 97.5)
- moved C43 6.75 mm to (162.2, 102.0)
- moved C44 6.75 mm to (162.2, 106.5)
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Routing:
- net VD: track 11.4 -> 707.0 mm, vias 106 -> 206
- net /VTEMP: track 278.2 -> 334.0 mm
- net Net-(U53--): track 4.92 -> 52.7 mm, vias 0 -> 5
- net Net-(U71--): track 4.95 -> 52.6 mm, vias 0 -> 5
- net Net-(U70--): track 4.95 -> 52.6 mm, vias 0 -> 5
- net Net-(U69--): track 4.95 -> 52.6 mm, vias 0 -> 5
- net Net-(U68--): track 4.95 -> 52.6 mm, vias 0 -> 5
- net Net-(U65--): track 4.95 -> 52.6 mm, vias 0 -> 5
- net Net-(U64--): track 4.95 -> 52.6 mm, vias 0 -> 5
- net Net-(U63--): track 4.95 -> 52.6 mm, vias 0 -> 5
- net Net-(U60--): track 4.95 -> 52.6 mm, vias 0 -> 5
- net Net-(U58--): track 4.95 -> 52.6 mm, vias 0 -> 5
- net Net-(U72--): track 4.95 -> 52.6 mm, vias 0 -> 5
- net Net-(U67--): track 4.95 -> 52.6 mm, vias 0 -> 5
- net Net-(U66--): track 4.95 -> 52.6 mm, vias 0 -> 5
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- removed copper zone on B.Cu, net VD
- removed copper zone on F.Cu, net VD
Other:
- board size 76.8 x 114 mm -> 76.8 x 112.2 mm
